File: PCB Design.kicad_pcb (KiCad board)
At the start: 4 copper layers, 43.5 x 30.5 mm, 17 parts, among them J1 Serial, J2 Digital Pins, J3 I2C, J4 ICSP, U1 24LC1025, U2 24LC1025, U3 DS1337, U4 ATMEGA328P-AU, Y1 Crystal 32MHz, Y2 Crystal 16MHz

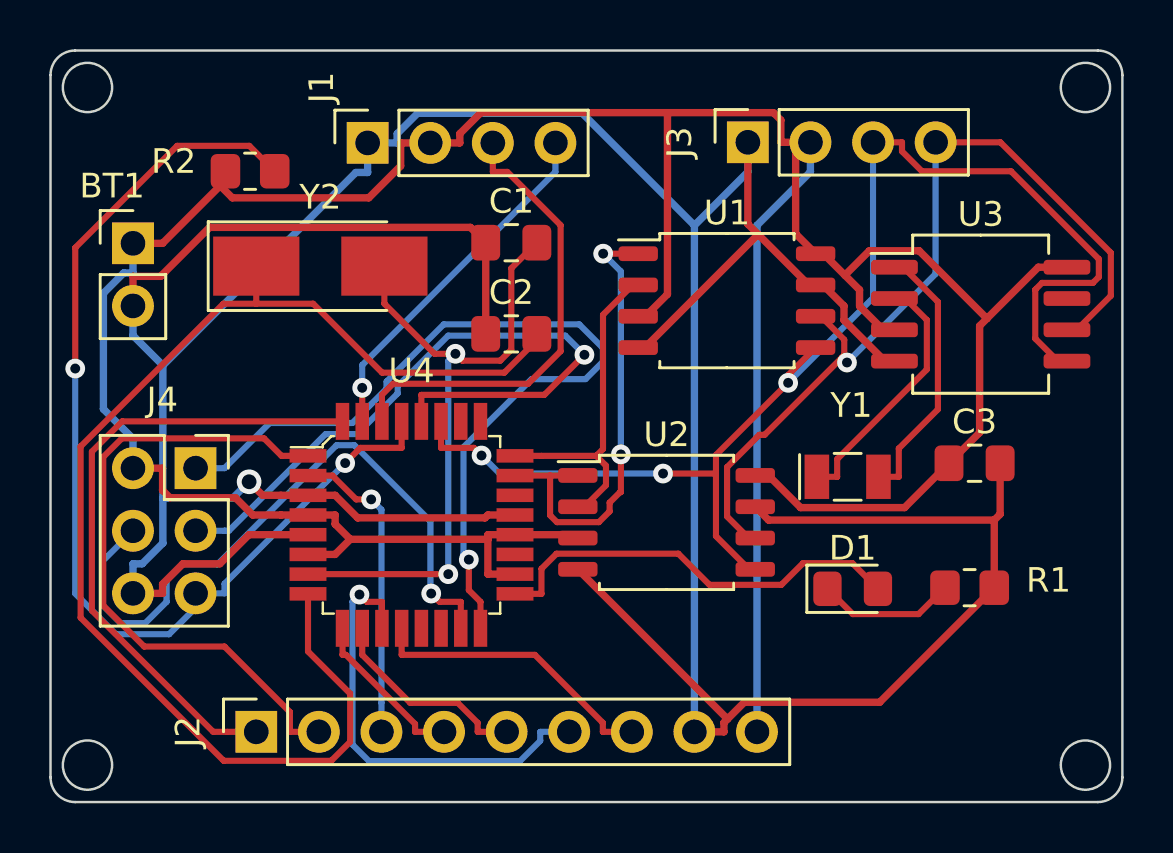
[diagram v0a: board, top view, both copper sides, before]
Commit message: add copper fill in 2 layered board
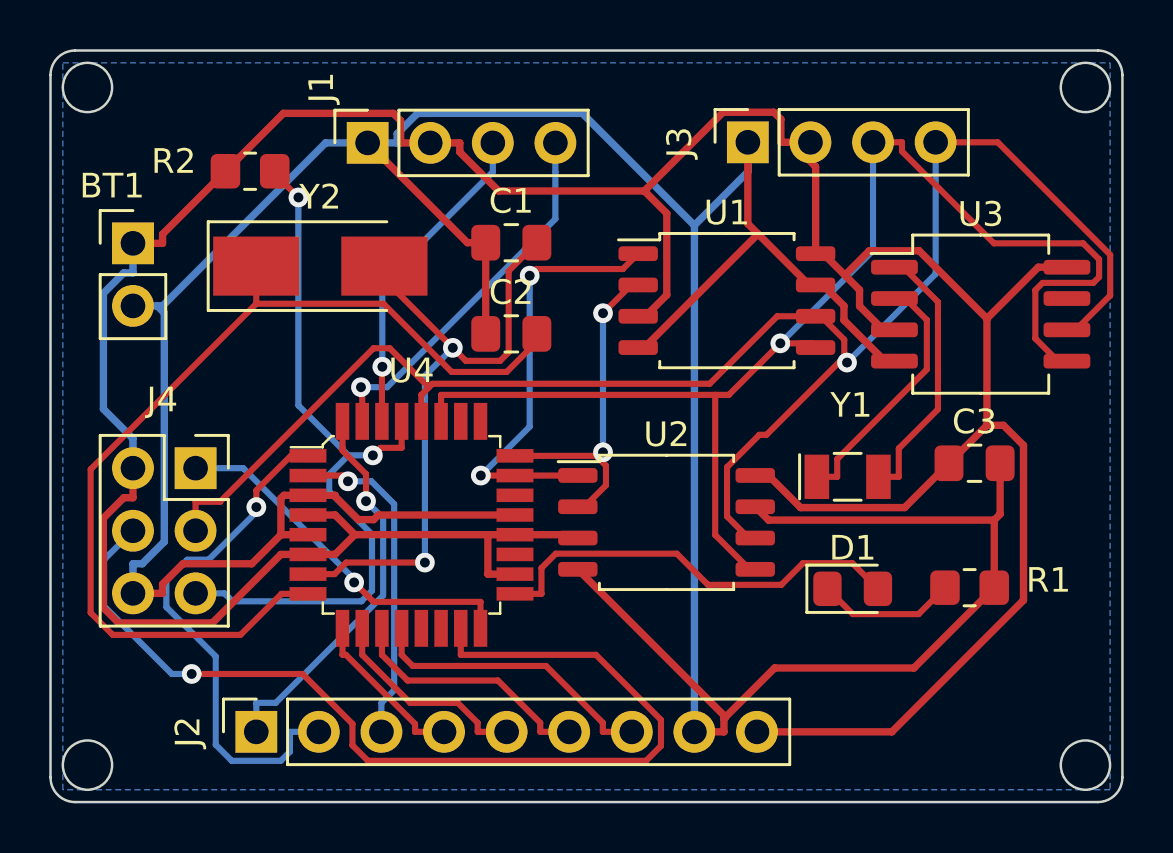
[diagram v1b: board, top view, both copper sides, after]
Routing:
- net /MISO: track 34.8 -> 15.0 mm
- net GNDPWR: track 167.3 -> 152.6 mm, vias 1 -> 0
- net /MOSI: track 27.3 -> 40.9 mm
- net /RESET: track 43.2 -> 30.1 mm
- net Net-(U4-Pad8): track 51.7 -> 40.1 mm
- net /D2: track 25.8 -> 15.9 mm, vias 0 -> 1
- net /D7: track 18.1 -> 10.2 mm, vias 1 -> 0
- net /SCK: track 74.8 -> 68.3 mm, vias 2 -> 1
- net /RX: track 19.0 -> 13.2 mm, vias 0 -> 1
- net /D3: track 26.3 -> 21.3 mm, vias 0 -> 1
- net /Vcc: track 138.2 -> 141.2 mm
- net /ADRS1: track 19.3 -> 17.6 mm
- net Net-(U4-Pad7): track 27.3 -> 26.1 mm
- net /D4: track 12.6 -> 13.4 mm
- net /TX: track 14.5 -> 15.2 mm
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- added copper zone on B.Cu, net GNDPWR
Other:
- copper layers 4 -> 2

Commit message: generate Gerber files and BOM
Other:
- board text added: "ATMEGA328P-AU"
- board text added: "Arduino Clone with: -EEPROM -Clock -I2C, SPI, GPIO"
- board text added: "D2"
- board text added: "D3"
- board text added: "D4"
- board text added: "D5"
- board text added: "D6"
- board text added: "D7"
- board text added: "D8"
- board text added: "Designed by Penguin"
- board text added: "GND"
- board text added: "MISO"
- board text added: "MOSI"
- board text added: "RST"
- board text added: "RX"
- board text added: "SCK"
- board text added: "SDA"
- board text added: "TX"
- board text added: "Vcc"
- board text added: "v1.0"
